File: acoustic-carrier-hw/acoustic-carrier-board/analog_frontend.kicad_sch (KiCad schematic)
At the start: 44 parts, among them IC1 ECP5-BGA256, J1 8P8C_Shielded, J7 Conn_02x08_Odd_Even, U3 MS9280

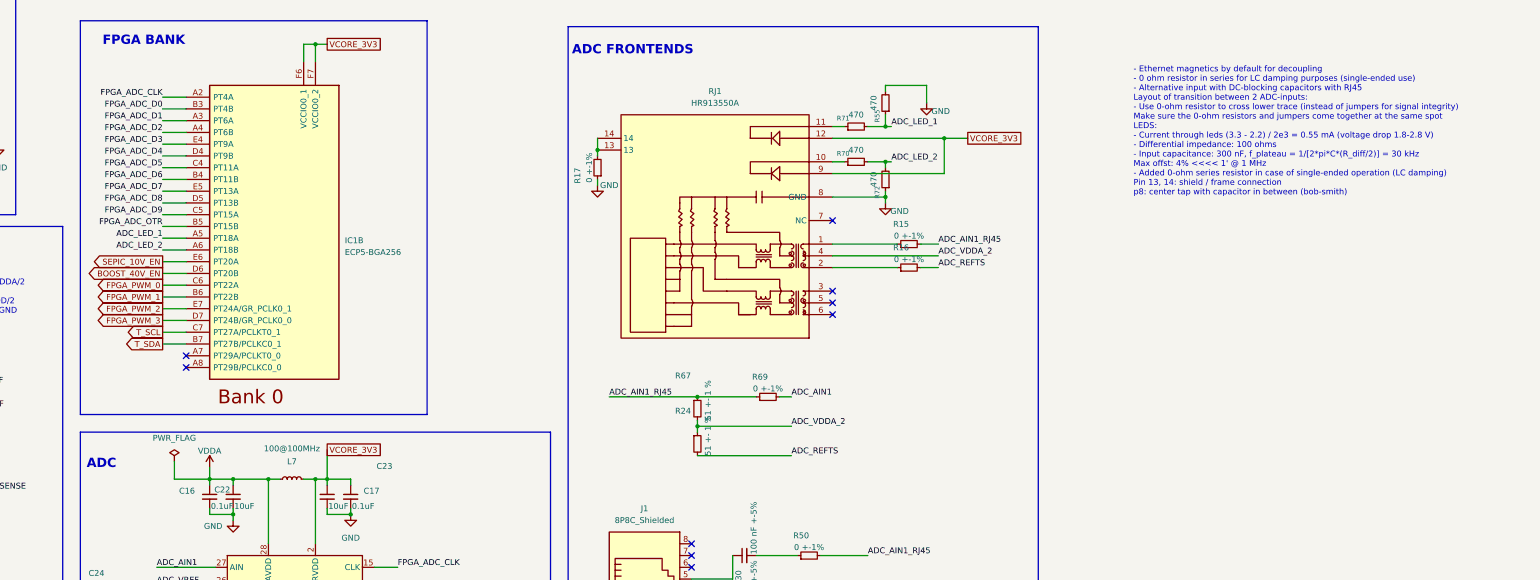
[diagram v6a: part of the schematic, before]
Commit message: [carrier] added rudimentary LC filter at input (next) - provision signal generator input
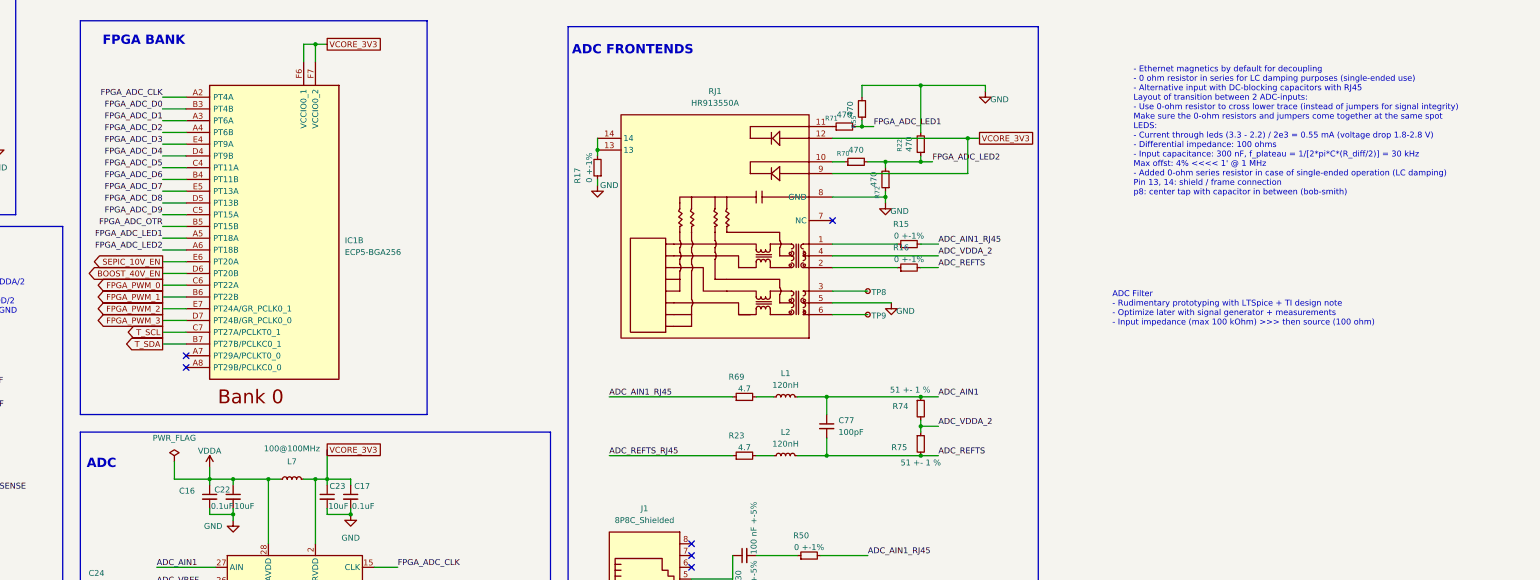
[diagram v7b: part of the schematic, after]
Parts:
- removed R24, R67: 51 +- 1 %, Resistor_SMD:R_0603_1608Metric_Pad0.98x0.95mm_HandSolder, symbol Device:R_Small
- added C77: 100pF, Capacitor_SMD:C_0603_1608Metric_Pad1.08x0.95mm_HandSolder, symbol Device:C_Small
- added L1, L2: 120nH, Inductor_SMD:L_0603_1608Metric_Pad1.05x0.95mm_HandSolder, symbol Device:L_Small
- added R22: 470, Resistor_SMD:R_0603_1608Metric, symbol Device:R_Small
- added R23: 4.7, Resistor_SMD:R_0603_1608Metric_Pad0.98x0.95mm_HandSolder, symbol Device:R_Small
- added R74, R75: 51 +- 1 %, Resistor_SMD:R_0603_1608Metric_Pad0.98x0.95mm_HandSolder, symbol Device:R_Small
- added TP8, TP9: TestPoint_Small, TestPoint:TestPoint_Pad_D1.5mm, symbol Connector:TestPoint_Small
- R69: value 0 +-1% -> 4.7; footprint Resistor_SMD:R_0805_2012Metric_Pad1.20x1.40mm_HandSolder -> Resistor_SMD:R_0603_1608Metric_Pad0.98x0.95mm_HandSolder; LPN 0805W8F0000T5E -> C23164; MPN C17477 -> 0603WAF470KT5E
- RJ1: LCSC Part C163507 -> (none)
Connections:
- net ADC_AIN1: now also C77.1, L1.2, R74.1; no longer R69.2
- net ADC_REFTS: now also C77.2, L2.2, R75.2
- net ADC_VDDA_2: now also R74.2, R75.1
- net GND: now also RJ1.5, R22.2
- net at RJ1.3: now also TP8.1
- net at RJ1.6: now also TP9.1
- net ADC_LED_1 renamed FPGA_ADC_LED1
- net ADC_LED_2 renamed FPGA_ADC_LED2
- net FPGA_ADC_LED2: now also R22.1
- new net: L1.1, R69.2
- new net: L2.1, R23.2
- new net ADC_REFTS_RJ45: R23.1
- no-connect marks 12 -> 9
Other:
- note added: "ADC Filter - Rudimentary prototyping with LTSpice + TI design note - Optimize later with signal generator + measurements - Input impedance (max 100 kOhm) >>> then source (100 ohm)"
- moved on the sheet: R55, R71

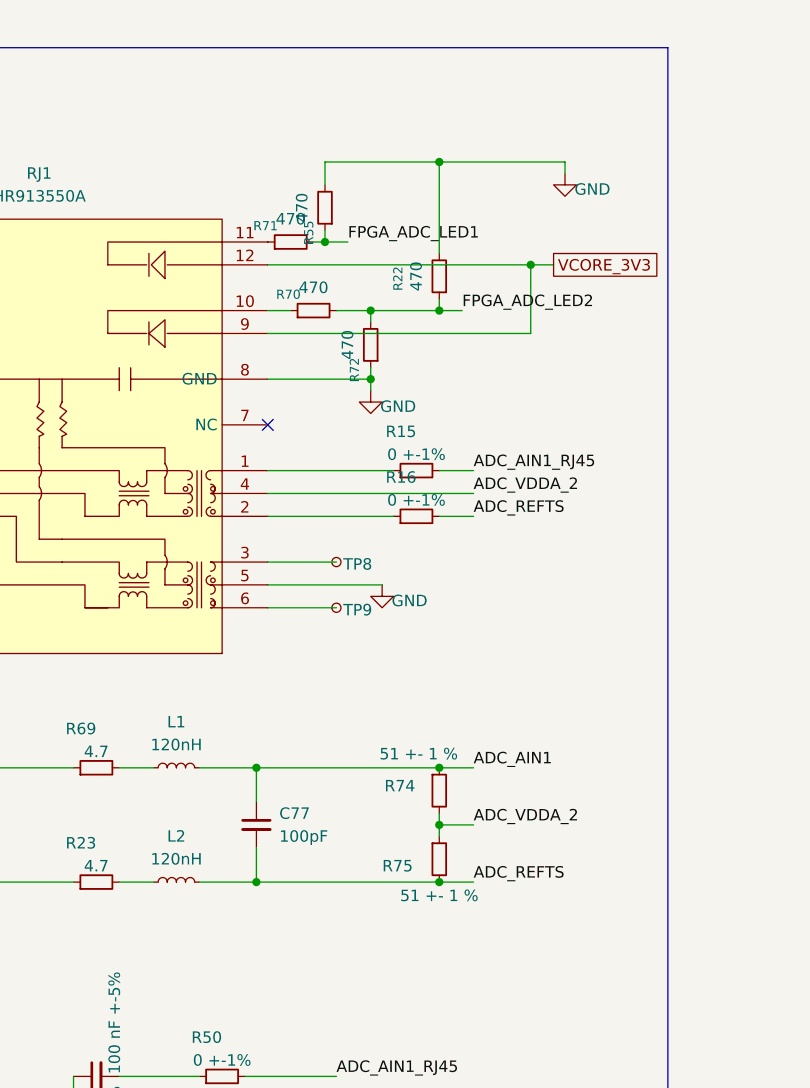
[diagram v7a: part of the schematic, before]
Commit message: [carrier] Fixed differential source impedance at simulation, added chebyshev + butterworth filters
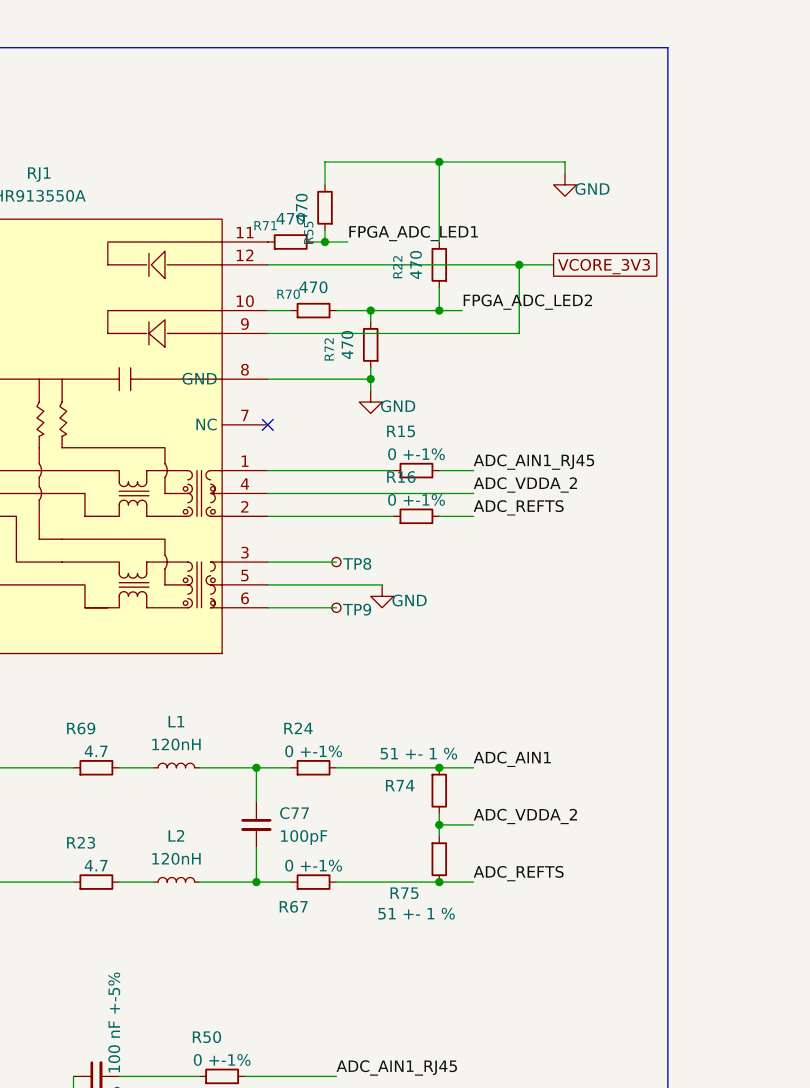
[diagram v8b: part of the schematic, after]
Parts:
- added R24, R67: 0 +-1%, Resistor_SMD:R_0805_2012Metric_Pad1.20x1.40mm_HandSolder, symbol Device:R_Small
- R74, R75: LPN 0603WAF510JT5E -> C23197; MPN C23197 -> 0603WAF510JT5E
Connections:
- net ADC_AIN1: now also R24.2; no longer C77.1, L1.2
- net ADC_REFTS: now also R67.2; no longer C77.2, L2.2
- new net: C77.1, L1.2, R24.1
- new net: C77.2, L2.2, R67.1
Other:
- moved on the sheet: R22
